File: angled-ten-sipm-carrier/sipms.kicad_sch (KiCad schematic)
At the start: 0 parts

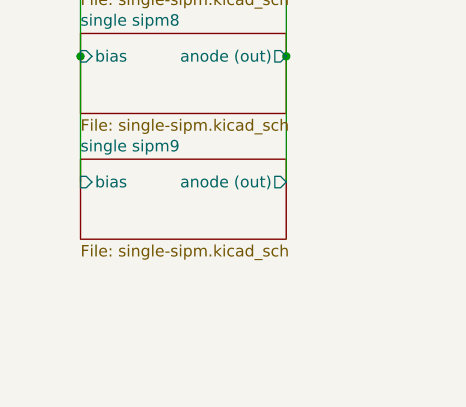
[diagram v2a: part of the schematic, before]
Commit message: eleven broadcom sipms
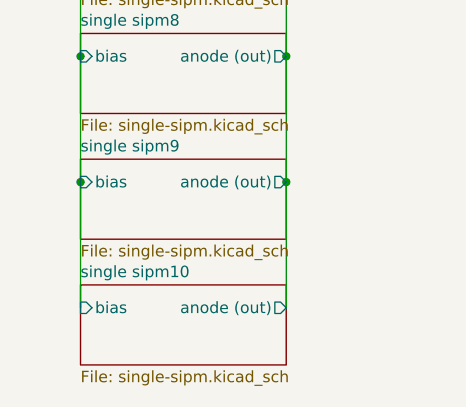
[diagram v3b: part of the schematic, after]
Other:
- added sheet single sipm10 (single-sipm.kicad_sch)
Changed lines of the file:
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@@
+	)
+	(junction
+		(at 35.56 168.91)
+		(diameter 0)
+		(color 0 0 0 0)
 	)
 	(junction
@@
 		(color 0 0 0 0)
 	)
+	(junction
+		(at 58.42 168.91)
+		(diameter 0)
+		(color 0 0 0 0)
+	)
+	(wire
+		(pts
+			(xy 58.42 57.15) (xy 58.42 71.12)
+		)
+		(stroke
+			(width 0)
+			(type default)
+		)
+	)
+	(wire
+		(pts
+			(xy 58.42 140.97) (xy 58.42 154.94)
+		)
+		(stroke
+			(width 0)
+			(type default)
+		)
+	)
+	(wire
+		(pts
+			(xy 58.42 35.56) (xy 58.42 43.18)
+		)
+		(stroke
+			(width 0)
+			(type default)
+		)
+	)
+	(wire
+		(pts
+			(xy 35.56 57.15) (xy 35.56 71.12)
+		)
+		(stroke
+			(width 0)
+			(type default)
+		)
+	)
+	(wire
+		(pts
+			(xy 62.23 35.56) (xy 58.42 35.56)
+		)
+		(stroke
+			(width 0)
+			(type default)
+		)
+	)
+	(wire
+		(pts
+			(xy 35.56 85.09) (xy 35.56 99.06)
+		)
+		(stroke
+			(width 0)
+			(type default)
+		)
+	)
+	(wire
+		(pts
+			(xy 58.42 154.94) (xy 58.42 168.91)
+		)
+		(stroke
+			(width 0)
+			(type default)
+		)
+	)
+	(wire
+		(pts
+			(xy 58.42 99.06) (xy 58.42 113.03)
+		)
+		(stroke
+			(width 0)
+			(type default)
+		)
+	)
+	(wire
+		(pts
+			(xy 35.56 31.75) (xy 35.56 43.18)
+		)
+		(stroke
+			(width 0)
+			(type default)
+		)
+	)
+	(wire
+		(pts
+			(xy 58.42 85.09) (xy 58.42 99.06)
+		)
+		(stroke
+			(width 0)
+			(type default)
+		)
+	)
 	(wire
 		(pts
@@
 	(wire
 		(pts
-			(xy 58.42 57.15) (xy 58.42 71.12)
+			(xy 35.56 43.18) (xy 35.56 57.15)
+		)
+		(stroke
+			(width 0)
+			(type default)
+		)
+	)
+	(wire
+		(pts
+			(xy 58.42 71.12) (xy 58.42 85.09)
+		)
+		(stroke
+			(width 0)
+			(type default)
+		)
+	)
+	(wire
+		(pts
+			(xy 58.42 168.91) (xy 58.42 182.88)
+		)
+		(stroke
+			(width 0)
+			(type default)
+		)
+	)
+	(wire
+		(pts
+			(xy 35.56 140.97) (xy 35.56 154.94)
 		)
 		(stroke
@@
 	(wire
 		(pts
-			(xy 58.42 35.56) (xy 58.42 43.18)
-		)
-		(stroke
-			(width 0)
-			(type default)
-		)
-	)
-	(wire
-		(pts
-			(xy 35.56 57.15) (xy 35.56 71.12)
-		)
-		(stroke
-			(width 0)
-			(type default)
-		)
-	)
-	(wire
-		(pts
-			(xy 62.23 35.56) (xy 58.42 35.56)
-		)
-		(stroke
-			(width 0)
-			(type default)
-		)
-	)
-	(wire
-		(pts
-			(xy 35.56 85.09) (xy 35.56 99.06)
-		)
-		(stroke
-			(width 0)
-			(type default)
-		)
-	)
-	(wire
-		(pts
-			(xy 58.42 99.06) (xy 58.42 113.03)
+			(xy 35.56 127) (xy 35.56 140.97)
 		)
 		(stroke
@@
 	(wire
 		(pts
-			(xy 35.56 31.75) (xy 35.56 43.18)
-		)
-		(stroke
-			(width 0)
-			(type default)
-		)
-	)
-	(wire
-		(pts
-			(xy 58.42 85.09) (xy 58.42 99.06)
-		)
-		(stroke
-			(width 0)
-			(type default)
-		)
-	)
-	(wire
-		(pts
-			(xy 58.42 154.94) (xy 58.42 168.91)
-		)
-		(stroke
-			(width 0)
-			(type default)
-		)
-	)
-	(wire
-		(pts
-			(xy 35.56 43.18) (xy 35.56 57.15)
-		)
-		(stroke
-			(width 0)
-			(type default)
-		)
-	)
-	(wire
-		(pts
-			(xy 58.42 71.12) (xy 58.42 85.09)
-		)
-		(stroke
-			(width 0)
-			(type default)
-		)
-	)
-	(wire
-		(pts
-			(xy 58.42 140.97) (xy 58.42 154.94)
+			(xy 35.56 71.12) (xy 35.56 85.09)
+		)
+		(stroke
+			(width 0)
+			(type default)
+		)
+	)
+	(wire
+		(pts
+			(xy 35.56 99.06) (xy 35.56 113.03)
+		)
+		(stroke
+			(width 0)
+			(type default)
+		)
+	)
+	(wire
+		(pts
+			(xy 58.42 43.18) (xy 58.42 57.15)
 		)
 		(stroke
@@
 	(wire
 		(pts
-			(xy 35.56 127) (xy 35.56 140.97)
-		)
-		(stroke
-			(width 0)
-			(type default)
-		)
-	)
-	(wire
-		(pts
-			(xy 35.56 71.12) (xy 35.56 85.09)
-		)
-		(stroke
-			(width 0)
-			(type default)
-		)
-	)
-	(wire
-		(pts
-			(xy 35.56 140.97) (xy 35.56 154.94)
-		)
-		(stroke
-			(width 0)
-			(type default)
-		)
-	)
-	(wire
-		(pts
-			(xy 35.56 99.06) (xy 35.56 113.03)
-		)
-		(stroke
-			(width 0)
-			(type default)
-		)
-	)
-	(wire
-		(pts
-			(xy 58.42 43.18) (xy 58.42 57.15)
+			(xy 35.56 168.91) (xy 35.56 182.88)
 		)
 		(stroke
@@
 				)
 			)
+		)
+	)
+	(sheet
+		(at 35.56 180.34)
+		(size 22.86 8.89)
+		(exclude_from_sim no)
+		(in_bom yes)
+		(on_board yes)
+		(dnp no)
+		(fields_autoplaced yes)
+		(stroke
+			(width 0.1524)
+			(type solid)
+		)
+		(fill
+			(color 0 0 0 0.0000)
+		)
+		(property "Sheetname" "single sipm10"
+			(at 35.56 179.6284 0)
+			(effects
+				(font
+					(size 1.27 1.27)
+				)
+				(justify left bottom)
+			)
+		)
+		(property "Sheetfile" "single-sipm.kicad_sch"
+			(at 35.56 189.8146 0)
+			(effects
+				(font
+					(size 1.27 1.27)
+				)
+				(justify left top)
+			)
+		)
+		(pin "bias" input
+			(at 35.56 182.88 180)
+			(effects
+				(font
+					(size 1.27 1.27)
+				)
+				(justify left)
+			)
+		)
+		(pin "anode (out)" output
+			(at 58.42 182.88 0)
+			(effects
+				(font
+					(size 1.27 1.27)
+				)
+				(justify right)
+			)
+		)
+		(instances
+			(project "10sipm-for-angled"
+				(path "/0ea1ec1f-35e4-4e8d-a06b-0b5fbc621c37/3c074e82-70e4-413f-9404-27bc853217d4"
+					(page "17")
+				)
+			)
